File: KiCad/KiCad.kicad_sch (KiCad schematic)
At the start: 130 parts, among them IC1 MCP23017-E_SO, IC2 MCP23017-E_SO, J1 Screw_Terminal_01x03, J10 Screw_Terminal_01x02, J11 Screw_Terminal_01x05, J12 Screw_Terminal_01x02, J13 Screw_Terminal_01x02, J14 Screw_Terminal_01x02, J15 Screw_Terminal_01x04, J16 Screw_Terminal_01x02, J17 Screw_Terminal_01x02, J18 Screw_Terminal_01x02, J19 Screw_Terminal_01x02, J2 Screw_Terminal_01x03, J3 Screw_Terminal_01x03, J4 Screw_Terminal_01x03, J5 Screw_Terminal_01x03, J6 Screw_Terminal_01x02, J7 Screw_Terminal_01x02, J8 Screw_Terminal_01x02, J9 Screw_Terminal_01x02, K1 2071556-9, K2 2071556-9, Q1 2N3906, Q10 2N3904, Q11 2N3904, Q12 2N3904, Q2 2N3906, Q3 2N3906, Q4 2N3906, Q5 2N3906, Q6 2N3904, Q7 2N3904, Q8 2N3904, Q9 2N3904, SW1 SW_Push, U1 L298HN, U2 ARDUINO_MKR_WAN_1310, U3 L298HN, U4 L298HN, U5 L298HN, U6 LM75AIMX_NOPB, U7 L7805

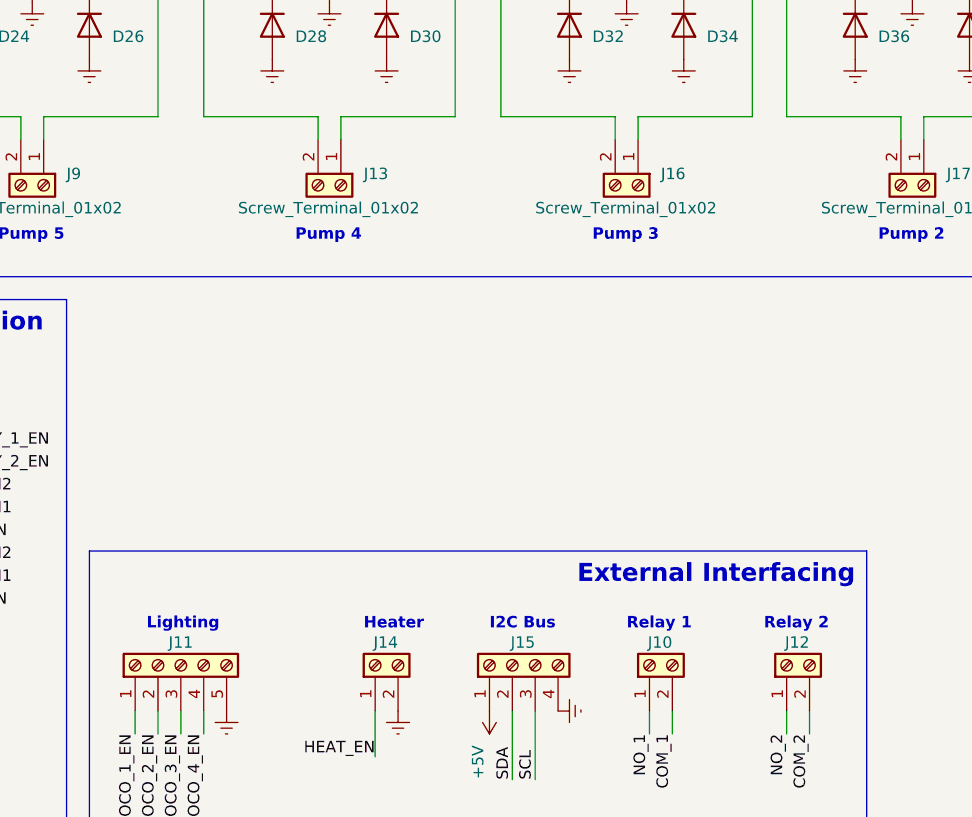
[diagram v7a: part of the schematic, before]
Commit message: added missing footprints
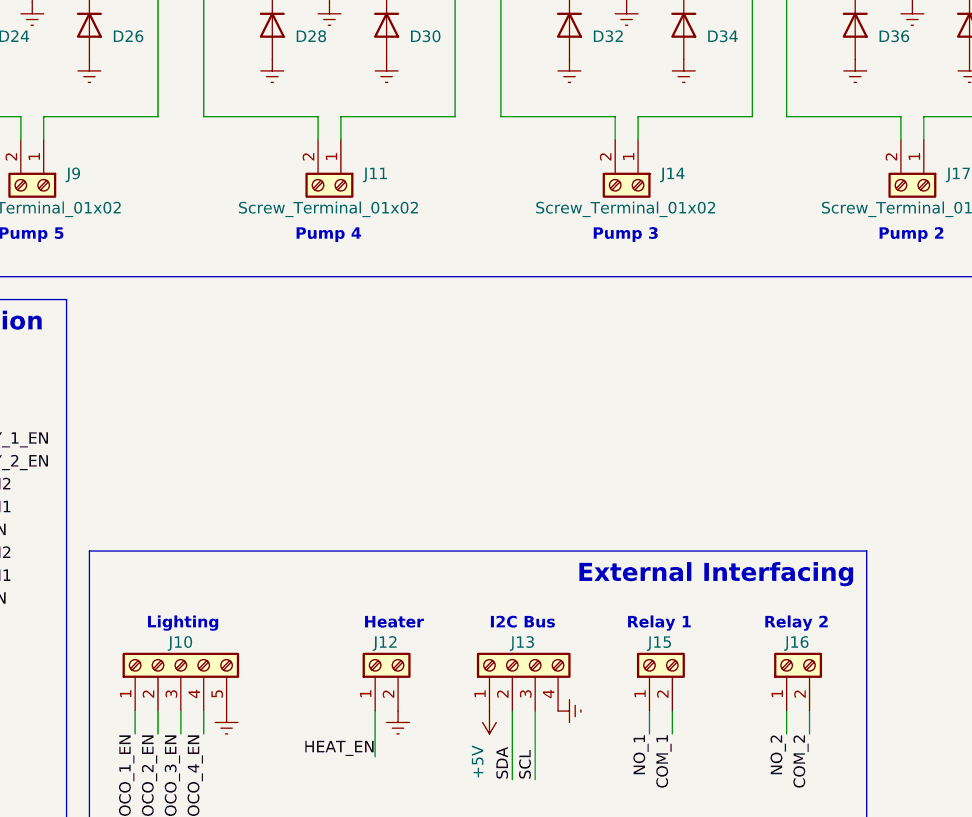
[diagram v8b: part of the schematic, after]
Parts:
- J10: renamed from J11; footprint (none) -> TerminalBlock_Phoenix:TerminalBlock_Phoenix_MKDS-1,5-5_1x05_P5.00mm_Horizontal
- K1, K2: footprint 20715569 -> SamacSys_Parts:20715569
- renumbered J13 to J11, J14 to J12, J15 to J13, J16 to J14, J10 to J15, J12 to J16
